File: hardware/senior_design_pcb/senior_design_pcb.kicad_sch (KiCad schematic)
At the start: 72 parts, among them J1 SBH11-PBPC-D05-ST-BK, J10 1x06Screw-Stepper Driver2, J11 2x08Rectangle-LED Matrix Conn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, J12 1x05JST - Joystick2 connector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, J13 UJ20-C-H-C-4-SMT-TR, J2 Conn_01x08_Pin, J3 1x02JST-IR Transmitter1, J4 1x03JST- IR Receiver1, J5 1x05JST-Admin LCD Console Con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, J6 1x05JST - Joystick1 connector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

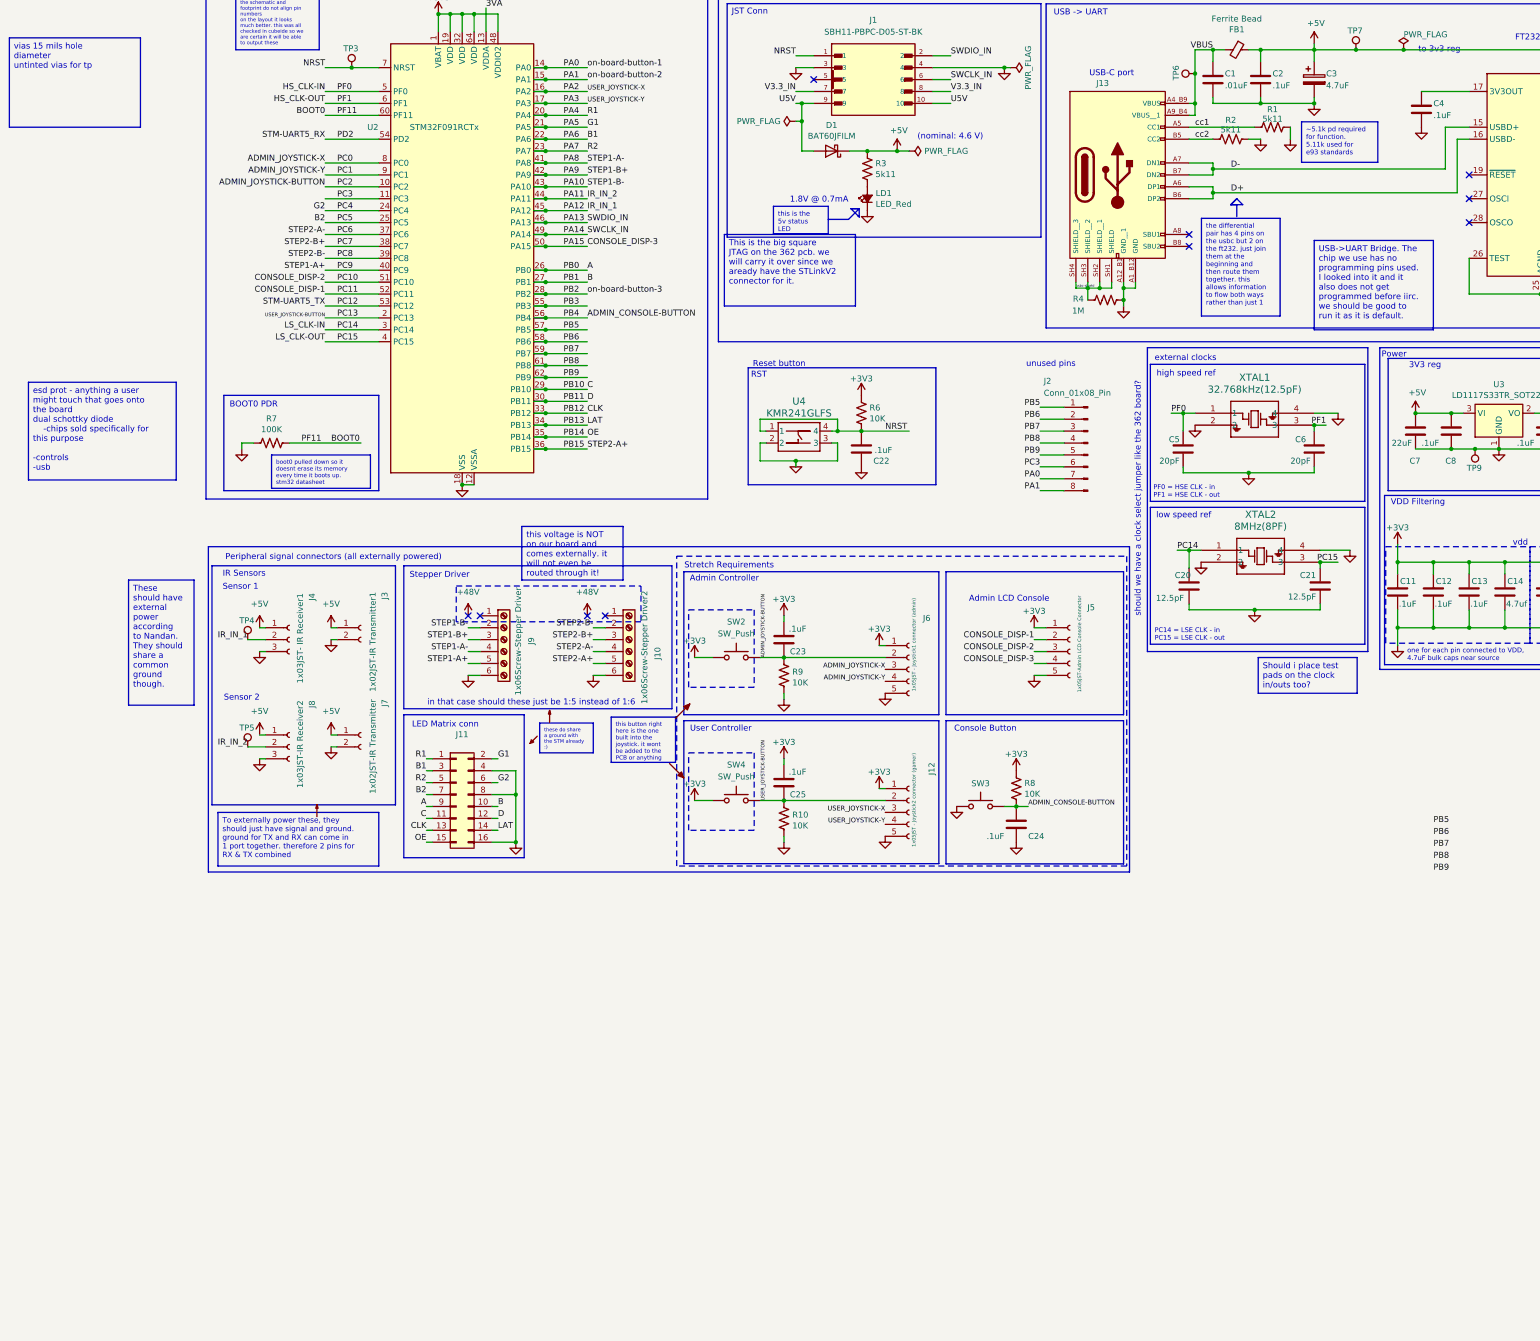
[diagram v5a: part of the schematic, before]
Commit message: added mosfets for driver control
added resistors
added labels
added comments
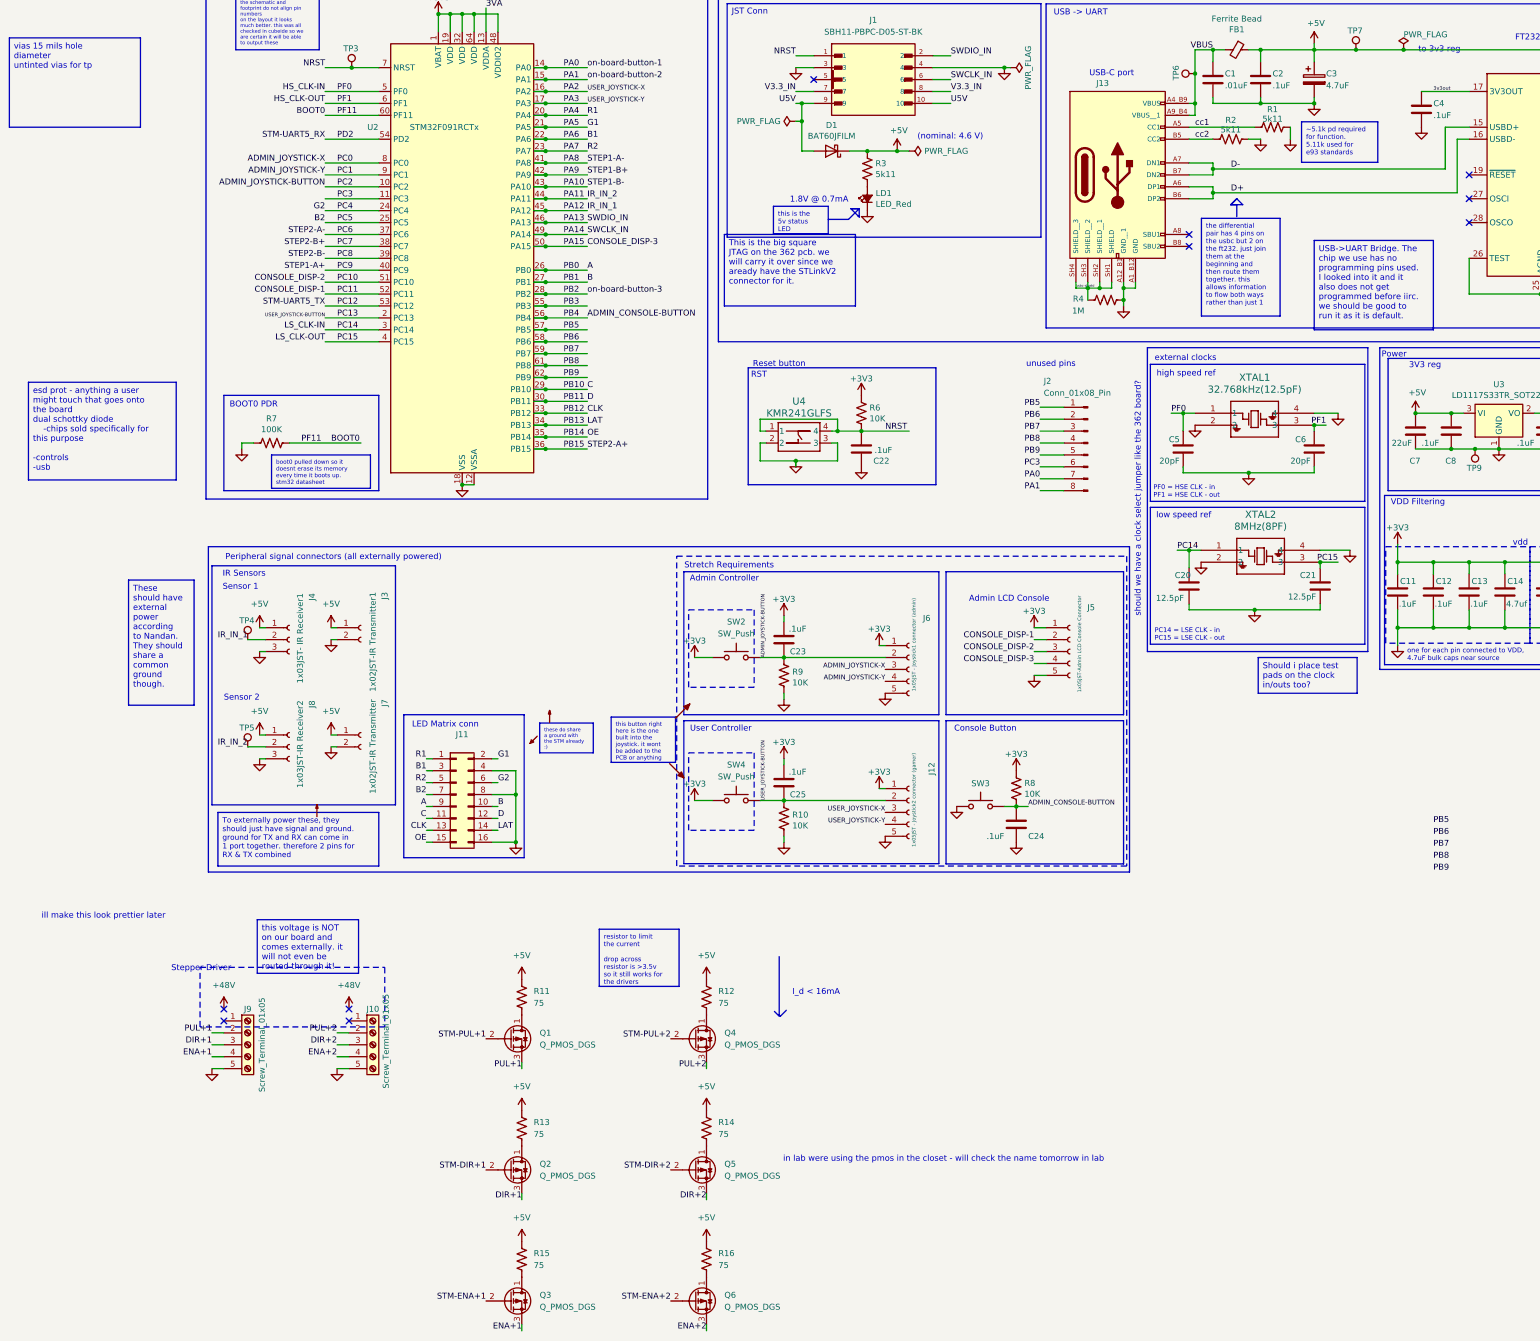
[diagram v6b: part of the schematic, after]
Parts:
- added Q1, Q2, Q3, Q4, Q5, Q6: Q_PMOS_DGS, symbol Transistor_FET:Q_PMOS_DGS
- added R11, R12, R13, R14, R15, R16: 75, symbol Device:R_US
- J10: value 1x06Screw-Stepper Driver2 -> Screw_Terminal_01x05; symbol Connector:Screw_Terminal_01x06 -> Connector:Screw_Terminal_01x05
- J9: value 1x06Screw-Stepper Driver -> Screw_Terminal_01x05; symbol Connector:Screw_Terminal_01x06 -> Connector:Screw_Terminal_01x05
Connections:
- net +5V: now also R11.1, R12.1, R13.1, R14.1, R15.1, R16.1
- net GND: now also J10.5 (Pin_5), J9.5 (Pin_5); no longer J10.6 (Pin_6), J9.6 (Pin_6)
- net PA10: no longer J9.2 (Pin_2)
- net PA8: no longer J9.4 (Pin_4)
- net PA9: no longer J9.3 (Pin_3)
- net PB15: no longer J10.5 (Pin_5)
- net PC6: no longer J10.4 (Pin_4)
- net PC7: no longer J10.3 (Pin_3)
- net PC8: no longer J10.2 (Pin_2)
- net PC9: no longer J9.5 (Pin_5)
- net 3v3out: now reaches C4.1, FT1.17 (3V3OUT)
- new net: Q3.1 (D), R15.2
- new net: Q1.1 (D), R11.2
- new net: Q5.1 (D), R14.2
- new net: Q6.1 (D), R16.2
- new net: Q4.1 (D), R12.2
- new net: Q2.1 (D), R13.2
- new net DIR+1: J9.3 (Pin_3), Q2.3 (S)
- new net DIR+2: J10.3 (Pin_3), Q5.3 (S)
- new net ENA+1: J9.4 (Pin_4), Q3.3 (S)
- new net ENA+2: J10.4 (Pin_4), Q6.3 (S)
- new net PUL+1: J9.2 (Pin_2), Q1.3 (S)
- new net PUL+2: J10.2 (Pin_2), Q4.3 (S)
- new net STM-DIR+1: Q2.2 (G)
- new net STM-DIR+2: Q5.2 (G)
- new net STM-ENA+1: Q3.2 (G)
- new net STM-ENA+2: Q6.2 (G)
- new net STM-PUL+1: Q1.2 (G)
- new net STM-PUL+2: Q4.2 (G)
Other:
- note added: "I_d < 16mA"
- note added: "ill make this look prettier later"
- note added: "in lab were using the pmos in the closet - will check the name tomorrow in lab"
- note removed: "in that case should these just be 1:5 instead of 1:6"

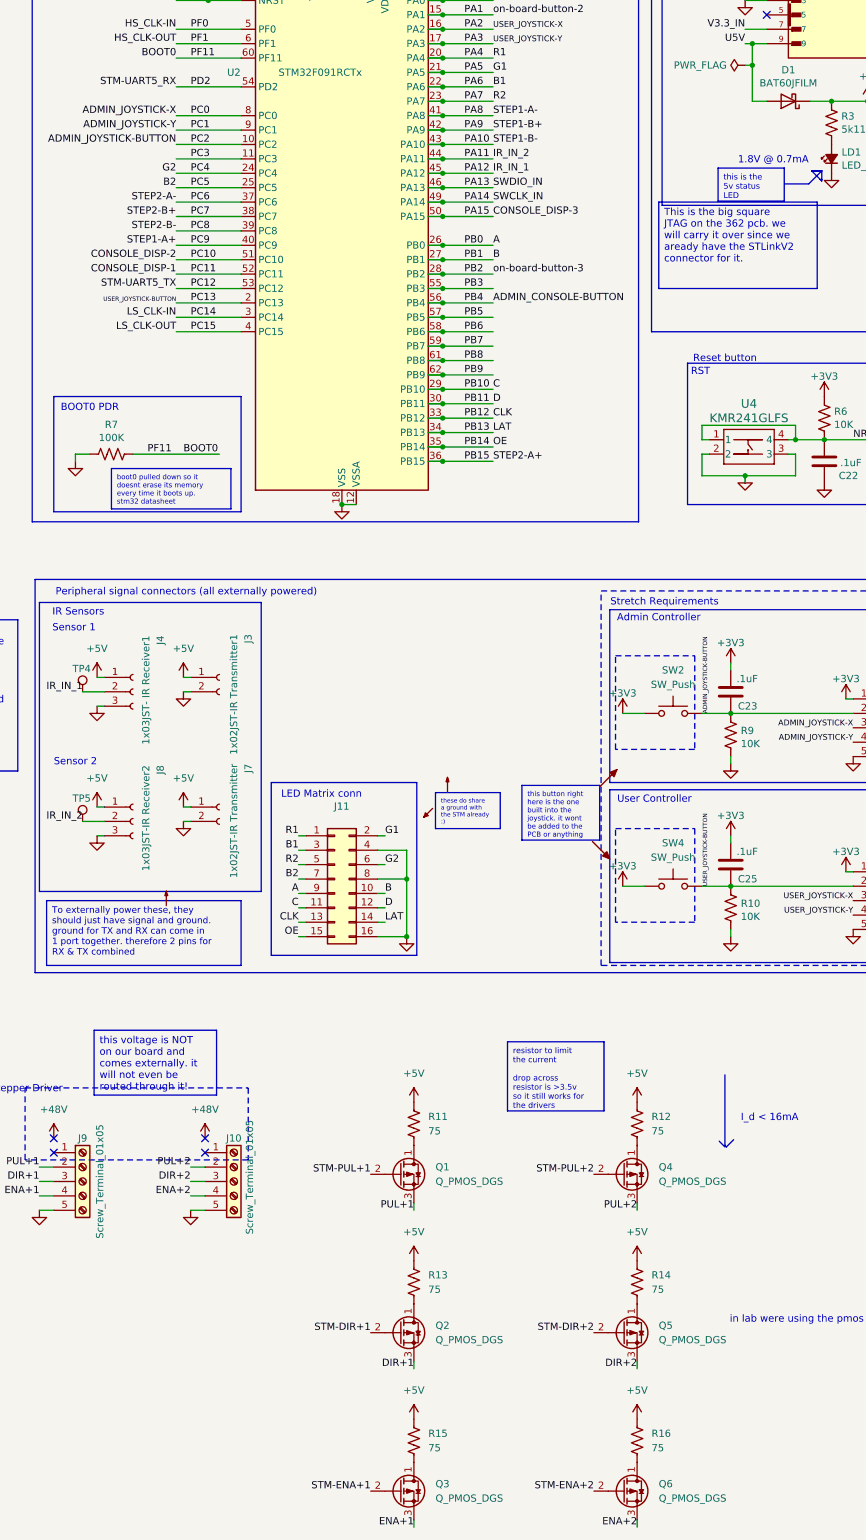
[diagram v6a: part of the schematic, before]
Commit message: Update senior_design_pcb.kicad_sch
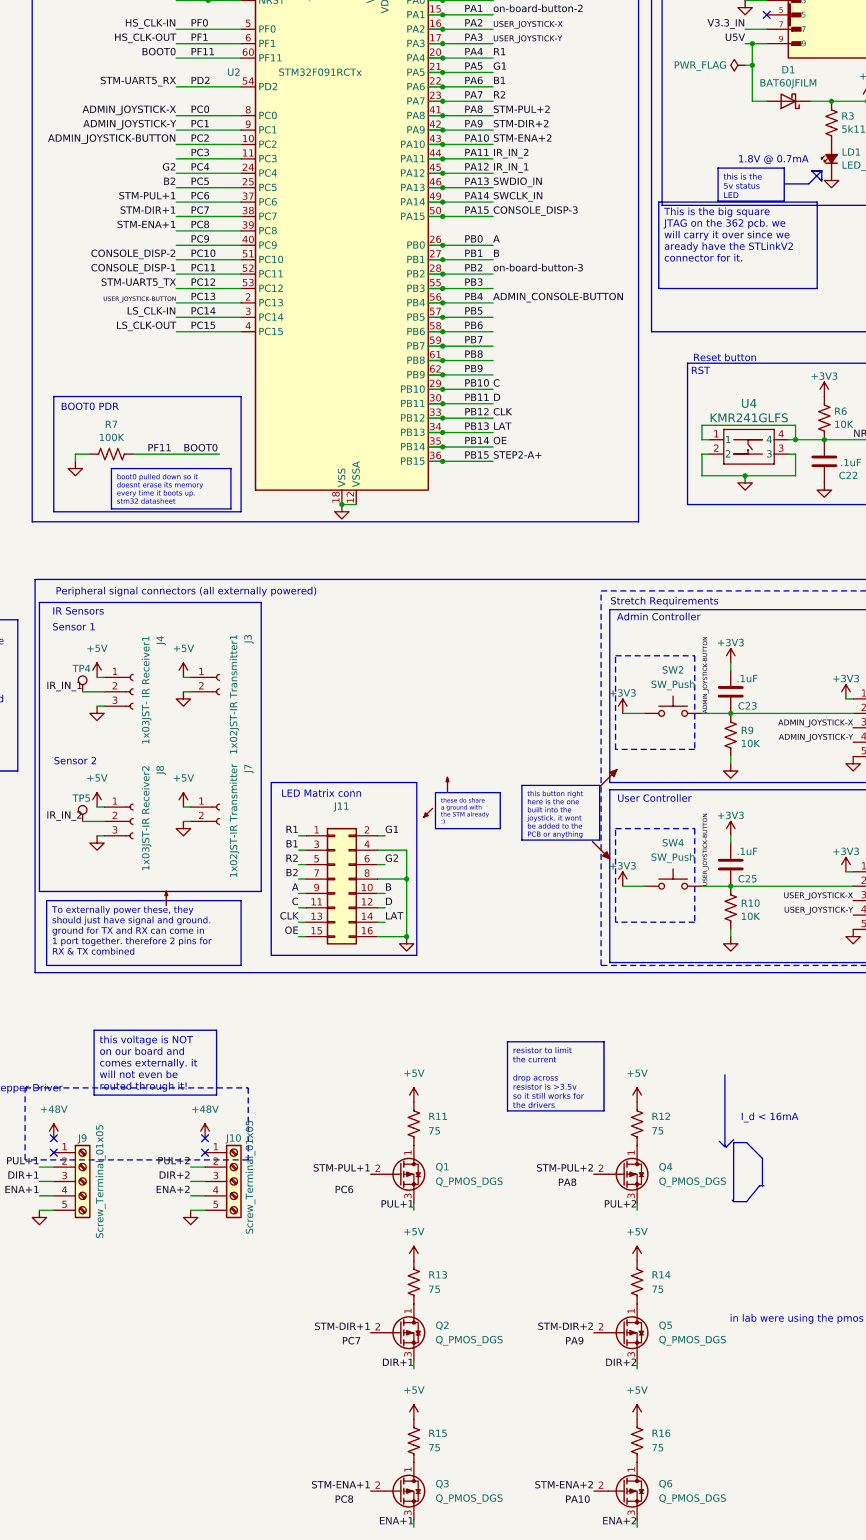
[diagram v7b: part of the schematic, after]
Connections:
- net STM-DIR+1 is gone; now on net PC7: Q2.2 (G)
- net STM-DIR+2 is gone; now on net PA9: Q5.2 (G)
- net STM-ENA+1 is gone; now on net PC8: Q3.2 (G)
- net STM-ENA+2 is gone; now on net PA10: Q6.2 (G)
- net STM-PUL+1 is gone; now on net PC6: Q1.2 (G)
- net STM-PUL+2 is gone; now on net PA8: Q4.2 (G)
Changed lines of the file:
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@@
 		)
 	)
+	(polyline
+		(pts
+			(xy 142.24 240.792) (xy 139.954 243.586)
+		)
+		(stroke
+			(width 0)
+			(type default)
+		)
+	)
 	(wire
 		(pts
@@
 		)
 	)
+	(polyline
+		(pts
+			(xy 142.24 240.792) (xy 143.002 240.792)
+		)
+		(stroke
+			(width 0)
+			(type default)
+		)
+	)
 	(wire
 		(pts
@@
 		)
 	)
+	(polyline
+		(pts
+			(xy 142.748 235.966) (xy 142.748 240.792)
+		)
+		(stroke
+			(width 0)
+			(type default)
+		)
+	)
 	(wire
 		(pts
@@
 		)
 	)
+	(polyline
+		(pts
+			(xy 139.954 243.586) (xy 137.668 243.586)
+		)
+		(stroke
+			(width 0)
+			(type default)
+		)
+	)
 	(wire
 		(pts
@@
 		)
 	)
+	(polyline
+		(pts
+			(xy 137.668 233.172) (xy 139.954 233.172)
+		)
+		(stroke
+			(width 0)
+			(type default)
+		)
+	)
 	(wire
 		(pts
@@
 		)
 	)
+	(polyline
+		(pts
+			(xy 139.954 233.172) (xy 142.748 235.966)
+		)
+		(stroke
+			(width 0)
+			(type default)
+		)
+	)
 	(wire
 		(pts
@@
 	(polyline
 		(pts
+			(xy 137.668 233.172) (xy 137.668 243.332)
+		)
+		(stroke
+			(width 0)
+			(type default)
+		)
+	)
+	(polyline
+		(pts
 			(xy 153.2089 63.3326) (xy 153.2089 63.5866)
 		)
@@
 		)
 	)
+	(polyline
+		(pts
+			(xy 137.414 243.332) (xy 137.668 243.586)
+		)
+		(stroke
+			(width 0)
+			(type default)
+		)
+	)
 	(wire
 		(pts
@@
 		)
 	)
+	(label "STM-ENA+2"
+		(at 95.25 57.15 0)
+		(effects
+			(font
+				(size 1.27 1.27)
+			)
+			(justify left bottom)
+		)
+	)
 	(label "PA0"
 		(at 90.17 31.75 0)
@@
 		)
 	)
+	(label "PC8"
+		(at 67.31 297.18 0)
+		(effects
+			(font
+				(size 1.27 1.27)
+			)
+			(justify left bottom)
+		)
+	)
 	(label "PB3"
 		(at 90.17 82.55 0)
@@
 		)
 	)
+	(label "PC6"
+		(at 67.31 242.57 0)
+		(effects
+			(font
+				(size 1.27 1.27)
+			)
+			(justify left bottom)
+		)
+	)
 	(label "SWCLK_IN"
 		(at 95.25 67.31 0)
@@
 		)
 	)
-	(label "STEP1-A-"
-		(at 95.25 52.07 0)
-		(effects
-			(font
-				(size 1.27 1.27)
-			)
-			(justify left bottom)
-		)
-	)
 	(label "U5V"
 		(at 172.72 39.37 0)
@@
 		)
 	)
+	(label "STM-PUL+2"
+		(at 95.25 52.07 0)
+		(effects
+			(font
+				(size 1.27 1.27)
+			)
+			(justify left bottom)
+		)
+	)
 	(label "IR_IN_1"
 		(at 95.25 62.23 0)
@@
 		)
 	)
-	(label "STEP2-B+"
-		(at 39.37 69.85 180)
-		(effects
-			(font
-				(size 1.27 1.27)
-			)
-			(justify right bottom)
-		)
-	)
 	(label "G2"
 		(at 39.37 62.23 180)
@@
 		)
 	)
-	(label "STEP2-A-"
-		(at 39.37 67.31 180)
-		(effects
-			(font
-				(size 1.27 1.27)
-			)
-			(justify right bottom)
-		)
-	)
 	(label "STM-PUL+2"
 		(at 113.03 238.76 180)
@@
 		)
 	)
-	(label "STEP1-A+"
-		(at 39.37 74.93 180)
-		(effects
-			(font
-				(size 1.27 1.27)
-			)
-			(justify right bottom)
-		)
-	)
 	(label "CONSOLE_DISP-2"
 		(at 39.37 77.47 180)
@@
 		)
 	)
-	(label "STEP1-B-"
-		(at 95.25 57.15 0)
+	(label "STM-DIR+1"
+		(at 39.37 69.85 180)
 		(effects
 			(font
 				(size 1.27 1.27)
 			)
-			(justify left bottom)
+			(justify right bottom)
 		)
 	)
@@
 		)
 	)
+	(label "PA10"
+		(at 107.95 297.18 0)
+		(effects
+			(font
+				(size 1.27 1.27)
+			)
+			(justify left bottom)
+		)
+	)
 	(label "CLK"
 		(at 60.96 194.31 180)
@@
 		)
 	)
+	(label "STM-PUL+1"
+		(at 39.37 67.31 180)
+		(effects
+			(font
+				(size 1.27 1.27)
+			)
+			(justify right bottom)
+		)
+	)
 	(label "PB8"
 		(at 275.59 200.66 0)
@@
 		)
 	)
+	(label "PA9"
+		(at 107.95 269.24 0)
+		(effects
+			(font
+				(size 1.27 1.27)
+			)
+			(justify left bottom)
+		)
+	)
 	(label "PB9"
 		(at 90.17 97.79 0)
@@
 		)
 	)
-	(label "STEP1-B+"
-		(at 95.25 54.61 0)
-		(effects
-			(font
-				(size 1.27 1.27)
-			)
-			(justify left bottom)
-		)
-	)
 	(label "PB0"
 		(at 90.17 74.93 0)
@@
 		)
 	)
+	(label "PA8"
+		(at 106.68 241.3 0)
+		(effects
+			(font
+				(size 1.27 1.27)
+			)
+			(justify left bottom)
+		)
+	)
 	(label "R2"
 		(at 60.96 184.15 180)
@@
 		)
 	)
+	(label "STM-ENA+1"
+		(at 39.37 72.39 180)
+		(effects
+			(font
+				(size 1.27 1.27)
+			)
+			(justify right bottom)
+		)
+	)
 	(label "ADMIN_JOYSTICK-Y"
 		(at 158.75 162.56 180)
@@
 		)
 	)
+	(label "STM-DIR+2"
+		(at 95.25 54.61 0)
+		(effects
+			(font
+				(size 1.27 1.27)
+			)
+			(justify left bottom)
+		)
+	)
 	(label "PB7"
 		(at 275.59 198.12 0)
@@
 		)
 	)
-	(label "STEP2-B-"
-		(at 39.37 72.39 180)
+	(label "PC7"
+		(at 68.58 269.24 0)
 		(effects
 			(font
 				(size 1.27 1.27)
 			)
-			(justify right bottom)
+			(justify left bottom)
 		)
 	)
